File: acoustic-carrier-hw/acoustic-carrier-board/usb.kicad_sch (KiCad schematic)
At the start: 59 parts, among them IC1 ECP5-BGA256, J6 USB-C connector, U15 USB3300-EZK, U18 LMV321, U6 TS3USB30EDGSR, Y3 Crystal_GND24_Small

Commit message: [carrier] Fixed error in ethernet power supply, separated footprints + symbols into library (next) check whether supply should be DVDDH
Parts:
- removed IC1: ECP5-BGA256, fpga:BGA256C80P16X16_1400X1400X170, symbol ecp5bga256:ECP5-BGA256
- removed J6: USB-C connector, Connector_USB:USB_C_Receptacle_HRO_TYPE-C-31-M-12, symbol USB_C:USB_C_Receptacle_USB2.0_16P
- removed U15: USB3300-EZK, fpga:QFN32_5X5MC_MCH, symbol USB3300-EZK:USB3300-EZK
- removed U16, U17, U19: ~, Package_TO_SOT_SMD:SOT-23-5, symbol COS3201:COS3201
- added IC1: ECP5-BGA256, iw-fpga_mcu:BGA256C80P16X16_1400X1400X170, symbol iw-fpga_mcu:ECP5-BGA256
- added J9: TYPE-C-31-M-12, Connector_USB:USB_C_Receptacle_HRO_TYPE-C-31-M-12, symbol iw-connector:TYPE-C-31-M-12
- added U12, U13, U15: ~, Package_TO_SOT_SMD:SOT-23-5, symbol iw-analog:COS3201
- added U7: USB3300-EZK, iw-phyctrl:QFN32_5X5MC_MCH, symbol iw-phyctrl:USB3300-EZK
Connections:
- net FPGA_CC1: now also IC1.R13 (PR41C)
- net FPGA_CC2: now also IC1.T14 (PR41D)
- net GND: now also J9.A1 (GND), J9.A12 (GND), J9.B1 (GND), J9.B12 (GND), J9.S1 (SHIELD), U12.2 (V-), U13.2 (V-), U15.2 (V-), U7.1 (GND), U7.2 (GND), U7.33 (EPAD)
- net USBDN1: now also J9.A7 (DN1)
- net USBDN2: now also J9.B7 (DN2)
- net USBDP1: now also J9.A6 (DP1)
- net USBDP2: now also J9.B6 (DP2)
- net USB_CC1: now also J9.A5 (CC1)
- net USB_CC2: now also J9.B5 (CC2)
- net USB_DM: now also U7.8 (DM)
- net USB_DP: now also U7.7 (DP)
- net USB_SENSE: now also IC1.R12 (PR44A/RDQS44)
- net USB_SW_VREF: now also U12.1 (-), U13.1 (-), U15.1 (-)
- net USB_ULPI.CLK: now also IC1.P15 (PR32B/RDQSN32), U7.14 (CLKOUT)
- net USB_ULPI.D0: now also IC1.R16 (PR35B/VREF1_3), U7.24 (DATA0)
- net USB_ULPI.D1: now also IC1.M13 (PR35C), U7.23 (DATA1)
- net USB_ULPI.D2: now also IC1.N14 (PR35D/RDQ32), U7.22 (DATA2)
- net USB_ULPI.D3: now also IC1.N13 (PR38A/RDQ44), U7.21 (DATA3)
- net USB_ULPI.D4: now also IC1.P14 (PR38B), U7.20 (DATA4)
- net USB_ULPI.D5: now also IC1.R15 (PR38C), U7.19 (DATA5)
- net USB_ULPI.D6: now also IC1.T15 (PR38D), U7.18 (DATA6)
- net USB_ULPI.D7: now also IC1.P13 (PR41A), U7.17 (DATA7)
- net USB_ULPI.DIR: now also IC1.M14 (PR32D), U7.12 (DIR)
- net USB_ULPI.NXT: now also IC1.P16 (PR35A), U7.11 (NXT)
- net USB_ULPI.RST: now also IC1.N16 (PR32A/RDQS32), U7.9 (RESET)
- net USB_ULPI.STP: now also IC1.L14 (PR32C), U7.13 (STP)
- net USB_VBUS: now also J9.A4 (VBUS), J9.A9 (VBUS), J9.B4 (VBUS), J9.B9 (VBUS), U12.5 (V+), U13.5 (V+), U15.5 (V+)
- net VCORE_3V3: now also IC1.K11 (VCCIO3_1), IC1.L11 (VCCIO3_2), U7.16 (VDD3.3), U7.25 (VDD3.3), U7.30 (VDD3.3), U7.31 (REG_EN), U7.6 (VDD3.3)
- net VDDA_USB1.8: now also U7.29 (VDDA1.8)
- net VDD_USB1.8: now also U7.15 (VDD1.8), U7.26 (VDD1.8)
- net at R38.1, R39.2: now also U7.28 (XI)
- net at R104.2: now also U7.32 (RBIAS)
- net at R119.2, R122.1: now also U15.4
- net at C117.2, R38.2, Y3.3: now also U7.27 (XO)
- net at R37.2: now also U7.4 (VBUS)
- net at D4.2 (A), R110.2: now also U13.4
- net at C96.1, R110.1, R111.2: now also U13.3 (+)
- net at C77.1, R48.2, R49.1: now also U12.3 (+)
- net at D2.2 (A), R49.2: now also U12.4
- net at R118.2, R119.1: now also U15.3 (+)
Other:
- moved on the sheet: R114, R115, R116, R117, R118, R119, R120, R121, R122, U18

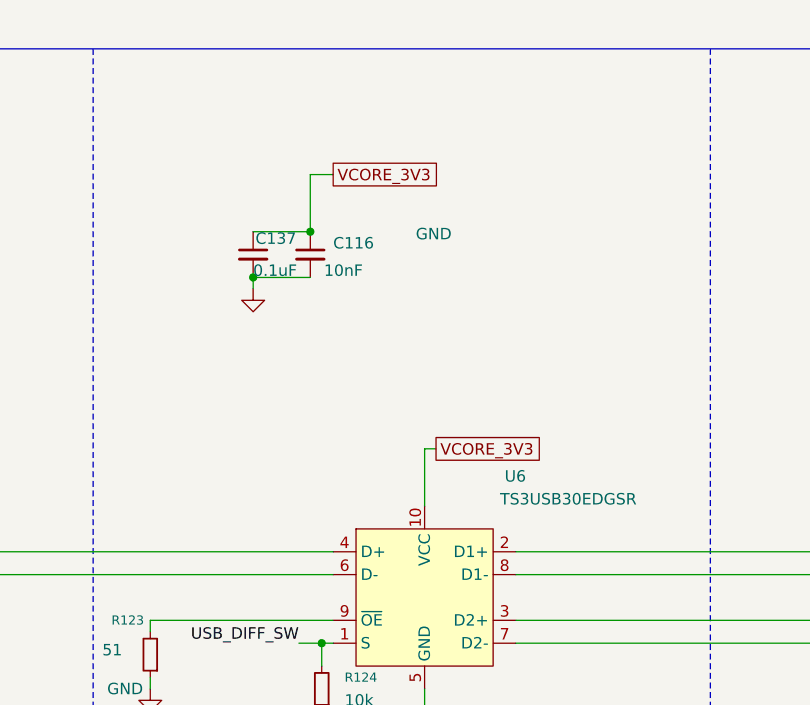
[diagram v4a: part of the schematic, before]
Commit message: [carrier] Signal switch-around in ddr3
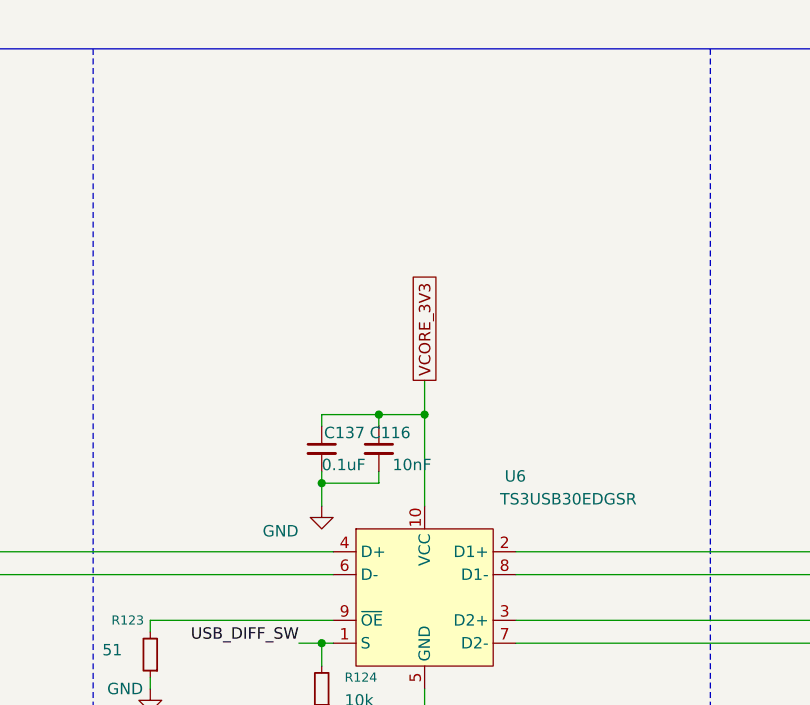
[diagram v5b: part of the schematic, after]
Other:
- moved on the sheet: C116, C137

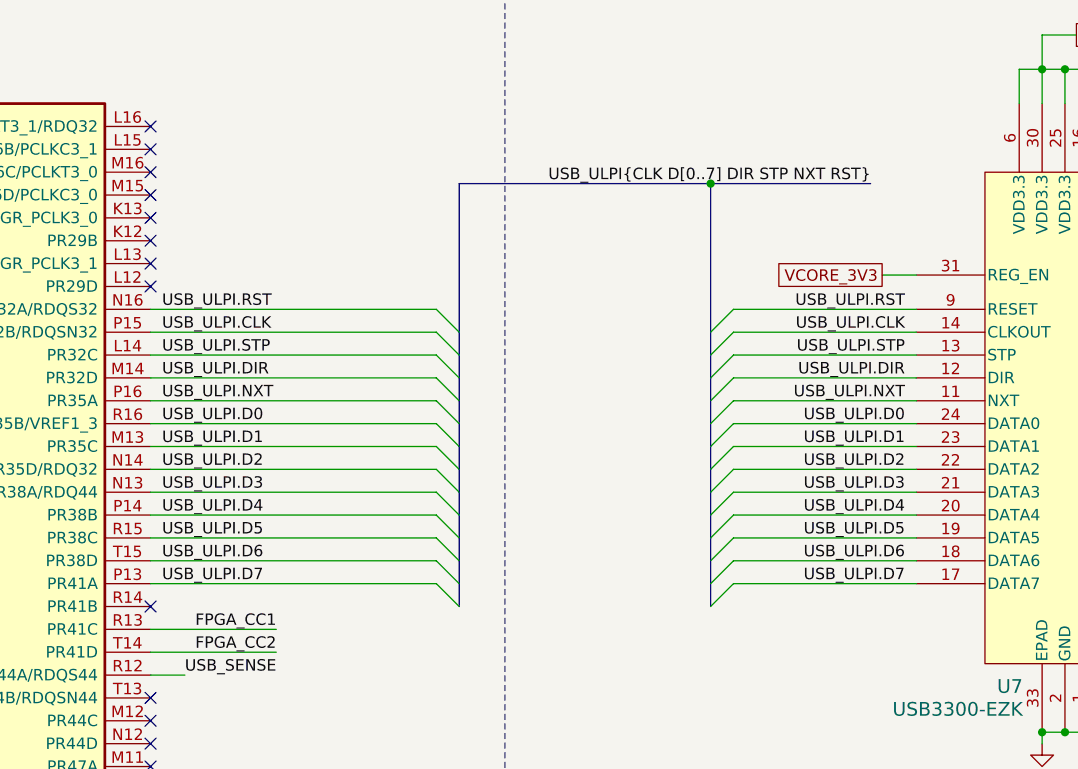
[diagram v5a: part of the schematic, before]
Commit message: [¢arrier] Fixed busses, added resistive arrays instead of 4x4k7 or 4x10k
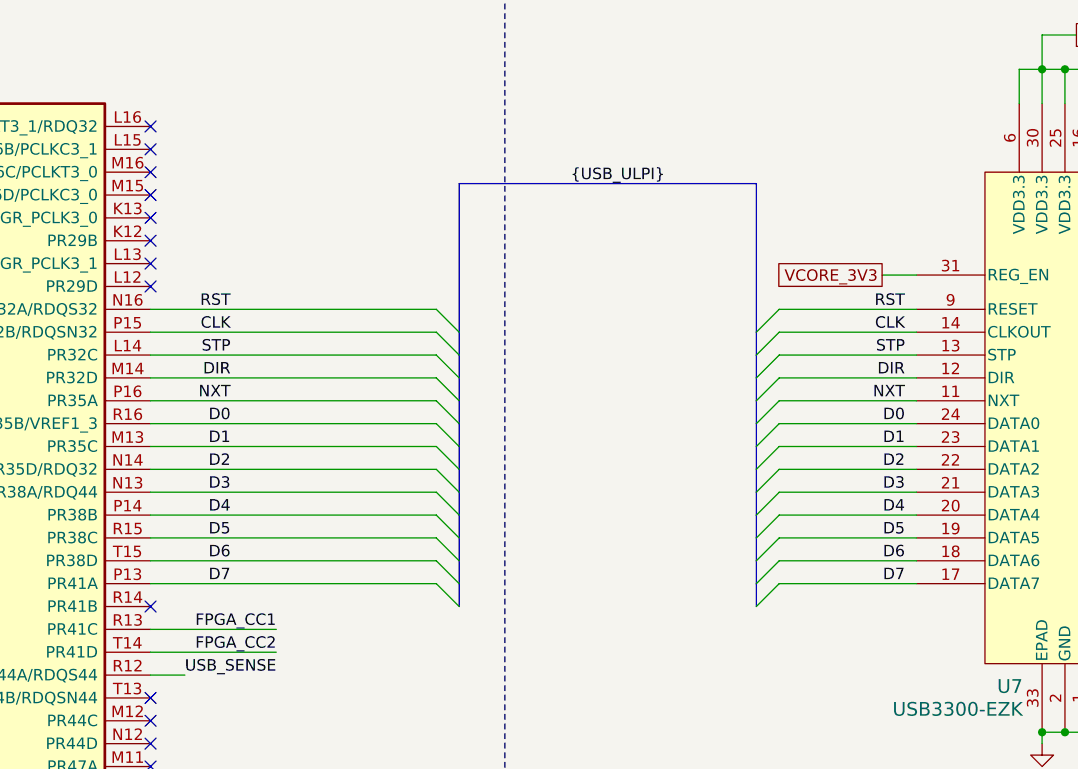
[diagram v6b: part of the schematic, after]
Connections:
- net USB_ULPI.CLK renamed CLK
- net USB_ULPI.D0 renamed D0
- net USB_ULPI.D1 renamed D1
- net USB_ULPI.D2 renamed D2
- net USB_ULPI.D3 renamed D3
- net USB_ULPI.D4 renamed D4
- net USB_ULPI.D5 renamed D5
- net USB_ULPI.D6 renamed D6
- net USB_ULPI.D7 renamed D7
- net USB_ULPI.DIR renamed DIR
- net USB_ULPI.NXT renamed NXT
- net USB_ULPI.RST renamed RST
- net USB_ULPI.STP renamed STP
